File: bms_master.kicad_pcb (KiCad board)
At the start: 4 copper layers, 85 x 65 mm, 104 parts, among them J1 Conn_01x02, J2 Conn_01x02, J3 Conn_01x02, J4 Conn_01x04, J5 Conn_01x04, J6 Conn_01x06, J7 Conn_01x05, J8 Conn_01x05, Q1 PMV15ENE, Q2 PMV74EPE, Q3 PMV74EPE, SW1 SW_Push, U1 TPS7B88, U10 TPS3851, U2 MCP1700x-330xxMB, U3 STM32F103C8Tx, U4 SN65HVD1050D, U5 M24C64-R, U6 MAX6126, U7 MAX11163, U8 741G3157, U9 TPS25961, Y1 8M

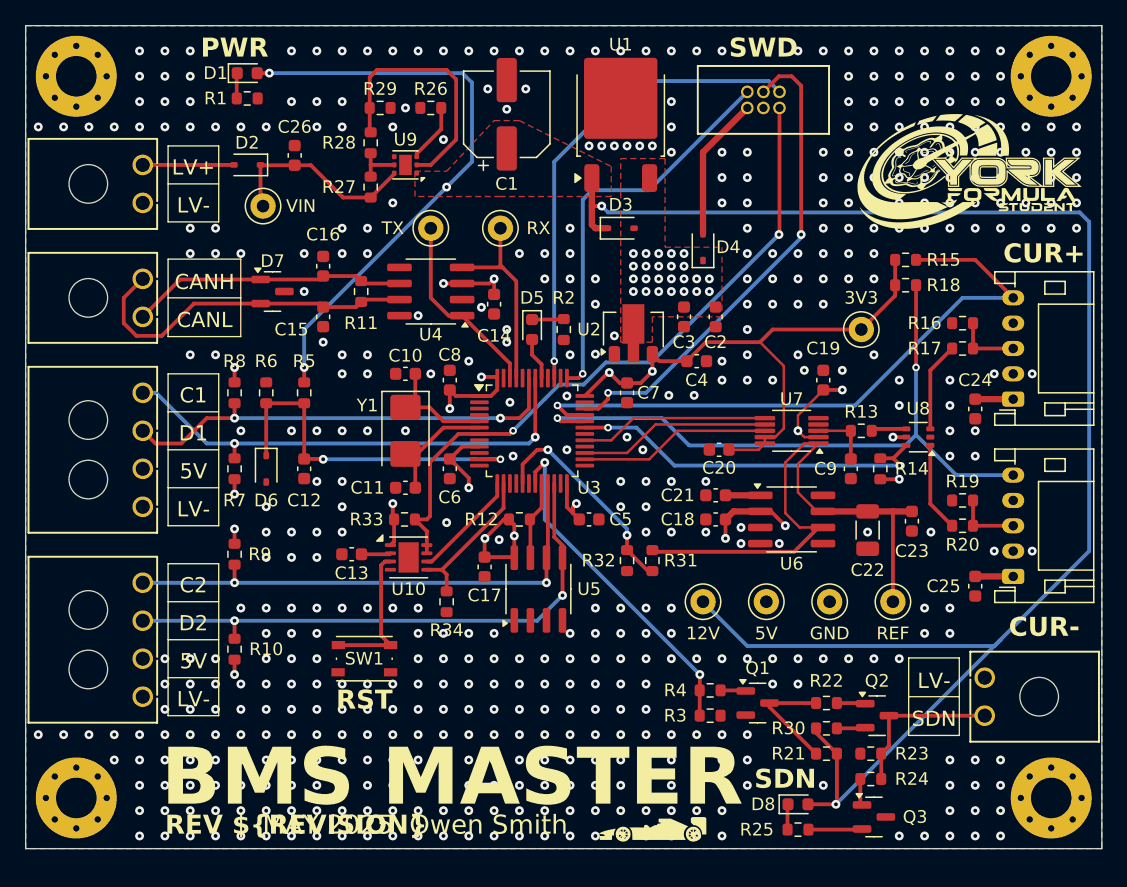
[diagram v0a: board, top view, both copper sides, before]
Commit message: pcb: Cleanup connector silkscreen
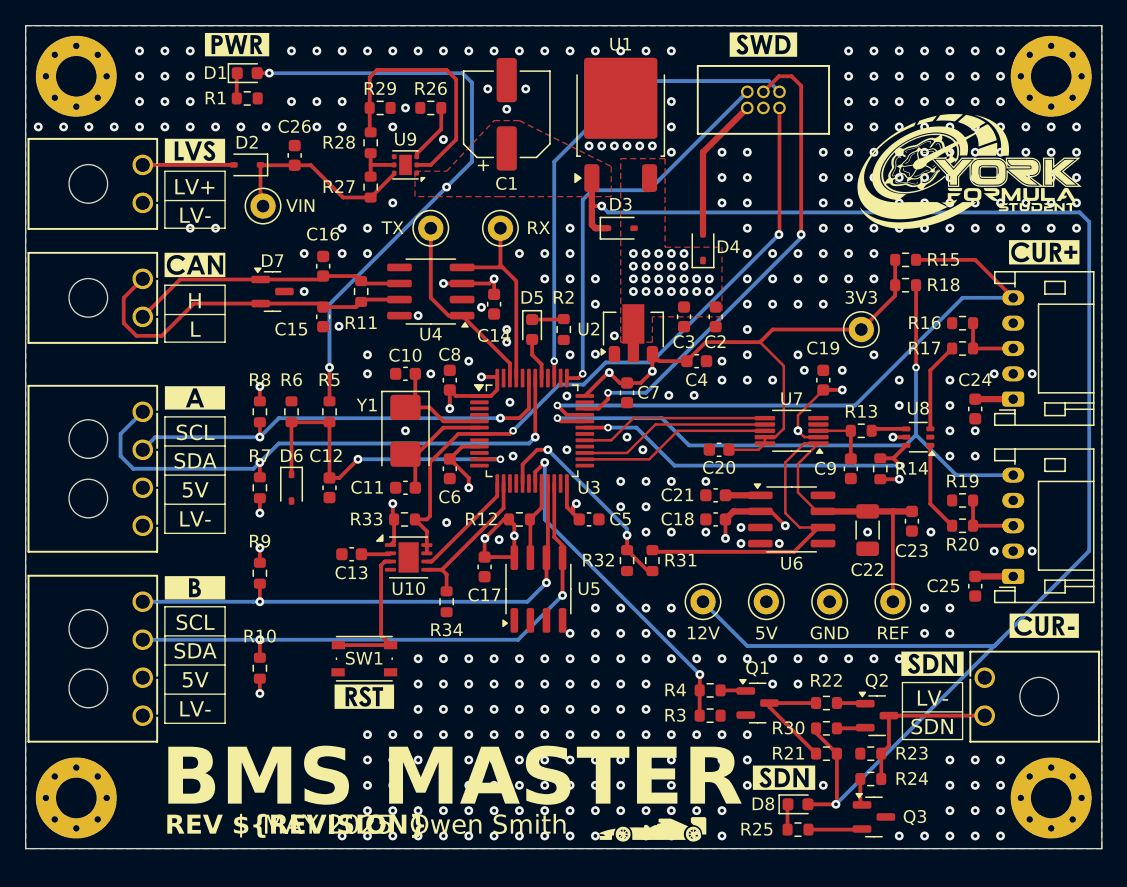
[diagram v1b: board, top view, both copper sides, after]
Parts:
- added kibuzzard-6910B743: G***, kibuzzard-6910B743, F.Cu at (78.4, 48.9)
- added kibuzzard-6910B7D7: G***, kibuzzard-6910B7D7, F.Cu at (78.4, 39.9)
- added kibuzzard-6910B84D: G***, kibuzzard-6910B84D, F.Cu at (78.4, 59.4)
- added kibuzzard-6910B859: G***, kibuzzard-6910B859, F.Cu at (78.4, 74.4)
- added kibuzzard-6910B9F6: G***, kibuzzard-6910B9F6, F.Cu at (124.9, 89.4)
- added kibuzzard-6910B9F6: G***, kibuzzard-6910B9F6, F.Cu at (136.6, 80.4)
- added kibuzzard-6910BA67: G***, kibuzzard-6910BA67, F.Cu at (145.4, 47.9)
- added kibuzzard-6910BA7C: G***, kibuzzard-6910BA7C, F.Cu at (145.4, 77.4)
- added kibuzzard-6910BB45: G***, kibuzzard-6910BB45, F.Cu at (91.8, 83.0)
- added kibuzzard-6910BB6B: G***, kibuzzard-6910BB6B, F.Cu at (81.7, 31.5)
- added kibuzzard-6910BB76: G***, kibuzzard-6910BB76, F.Cu at (123.3, 31.5)
- moved C12 2.50 mm to (89.0, 66.5)
- moved D6 2.50 mm to (86.0, 66.5)
- moved R10 2.50 mm to (83.5, 80.8)
- moved R5 2.50 mm to (89.0, 60.5)
- moved R6 2.50 mm to (86.0, 60.5)
- moved R7 2.50 mm to (83.5, 66.5)
- moved R8 2.50 mm to (83.5, 60.5)
- moved R9 2.50 mm to (83.5, 73.2)
- moved J4 1.50 mm to (74.2, 69.5)
- moved J5 1.50 mm to (74.2, 84.5)
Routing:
- net SCL1: track 38.7 -> 44.3 mm
- net Net-(D6-K): track 28.7 -> 27.3 mm
- net +12V: track 179.6 -> 180.3 mm
- net SDA2: track 44.5 -> 45.1 mm
- net SCL2: track 41.2 -> 41.8 mm
- net GND: vias 495 -> 378
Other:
- board text added: "H"
- board text added: "L"
- board text added: "SCL"
- board text added: "SDA"
- board text removed: "C1"
- board text removed: "C2"
- board text removed: "CANH"
- board text removed: "CANL"
- board text removed: "CUR+"
- board text removed: "CUR-"
- board text removed: "D1"
- board text removed: "D2"
- board text removed: "PWR"
- board text removed: "RST"
- board text removed: "SWD"

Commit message: *: Reorder reference designators
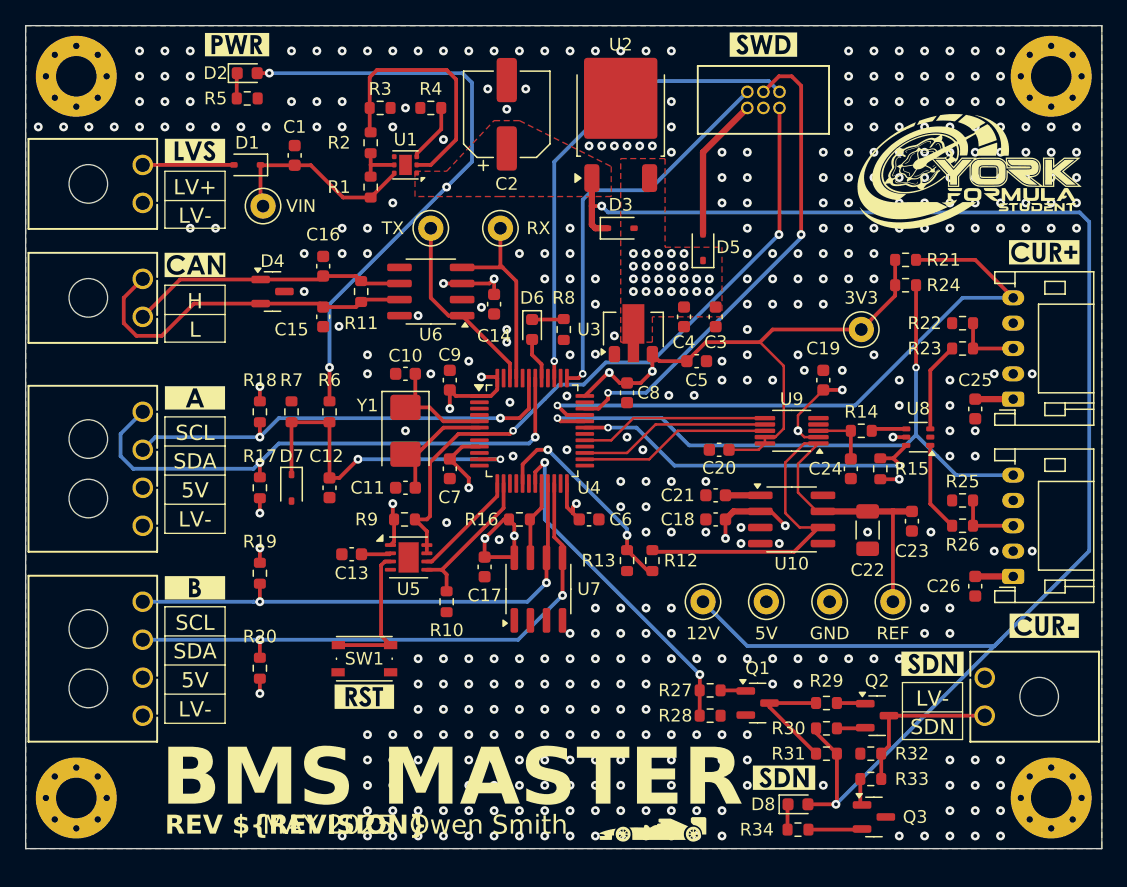
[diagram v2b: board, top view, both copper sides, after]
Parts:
- renumbered C26 to C1, C1 to C2, C9 to C24, C24 to C25, C25 to C26, C2 to C3, C3 to C4, C4 to C5, C5 to C6, C6 to C7, C7 to C8, C8 to C9, D2 to D1, D1 to D2, D7 to D4, D4 to D5, D5 to D6, D6 to D7, R27 to R1, R34 to R10, R31 to R12, R32 to R13, R13 to R14, R14 to R15, R12 to R16, R7 to R17, R8 to R18, R9 to R19, R28 to R2, R10 to R20, R15 to R21, R16 to R22, R17 to R23, R18 to R24, R19 to R25, R20 to R26, R4 to R27, R3 to R28, R22 to R29, R29 to R3, R21 to R31, R23 to R32, R24 to R33, R25 to R34, R26 to R4, R1 to R5, R5 to R6, R6 to R7, R2 to R8, R33 to R9, U9 to U1, U6 to U10, U1 to U2, U2 to U3, U3 to U4, U10 to U5, U4 to U6, U5 to U7, U7 to U9

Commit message: pcb: Cleanup vias and designator silkscreen
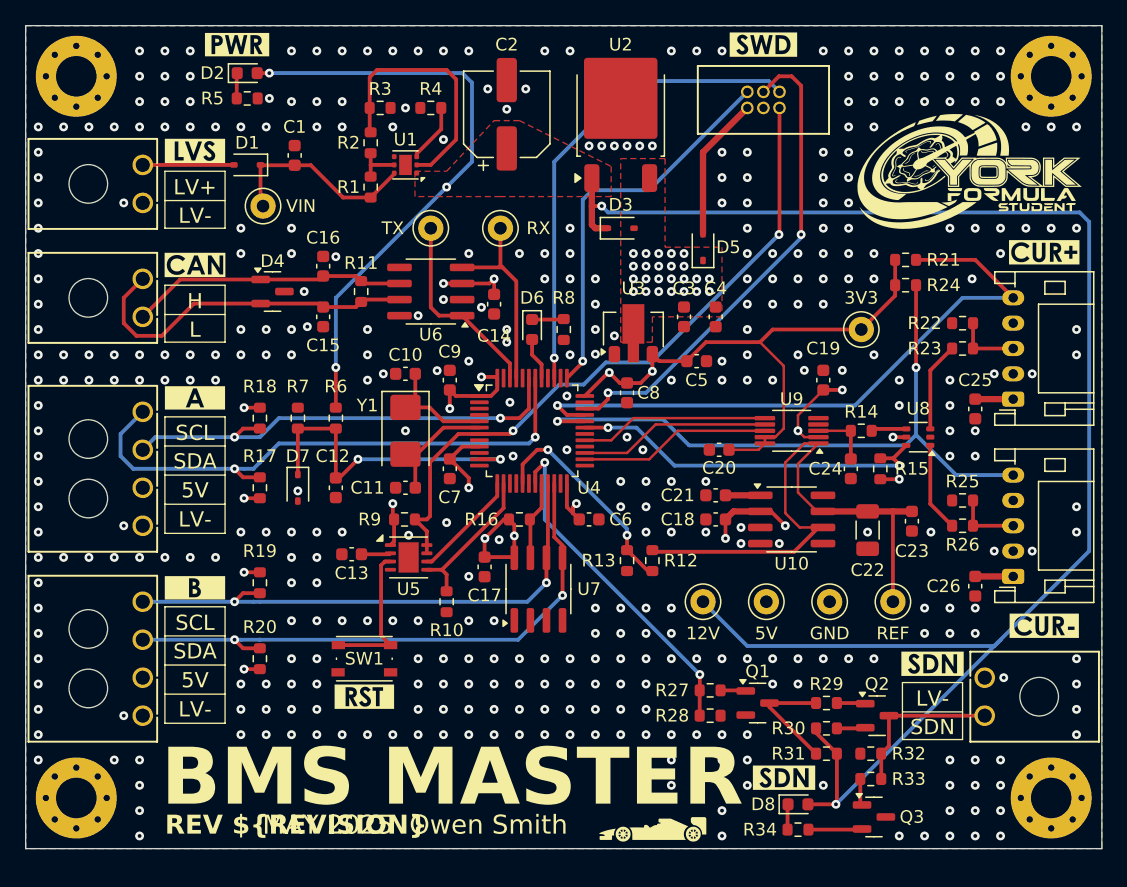
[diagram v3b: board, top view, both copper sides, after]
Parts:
- moved C3 2.50 mm to (117.0, 53.0)
- moved C4 2.50 mm to (119.5, 53.0)
- moved R19 0.75 mm to (83.5, 74.0)
- moved R20 0.75 mm to (83.5, 80.0)
- moved R6 0.71 mm to (89.5, 61.0)
- moved R7 0.71 mm to (86.5, 61.0)
- moved C12 0.50 mm to (89.5, 66.5)
- moved D7 0.50 mm to (86.5, 66.5)
- moved R18 0.50 mm to (83.5, 61.0)
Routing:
- net Net-(D7-K): track 27.3 -> 25.8 mm
- net SCL1: track 44.3 -> 45.4 mm
- net SDA1: track 35.4 -> 36.5 mm
- net SDA2: track 45.1 -> 46.0 mm
- net SCL2: track 41.8 -> 42.7 mm
- net /SWCLK: track 31.7 -> 31.1 mm
- net GND: vias 378 -> 395

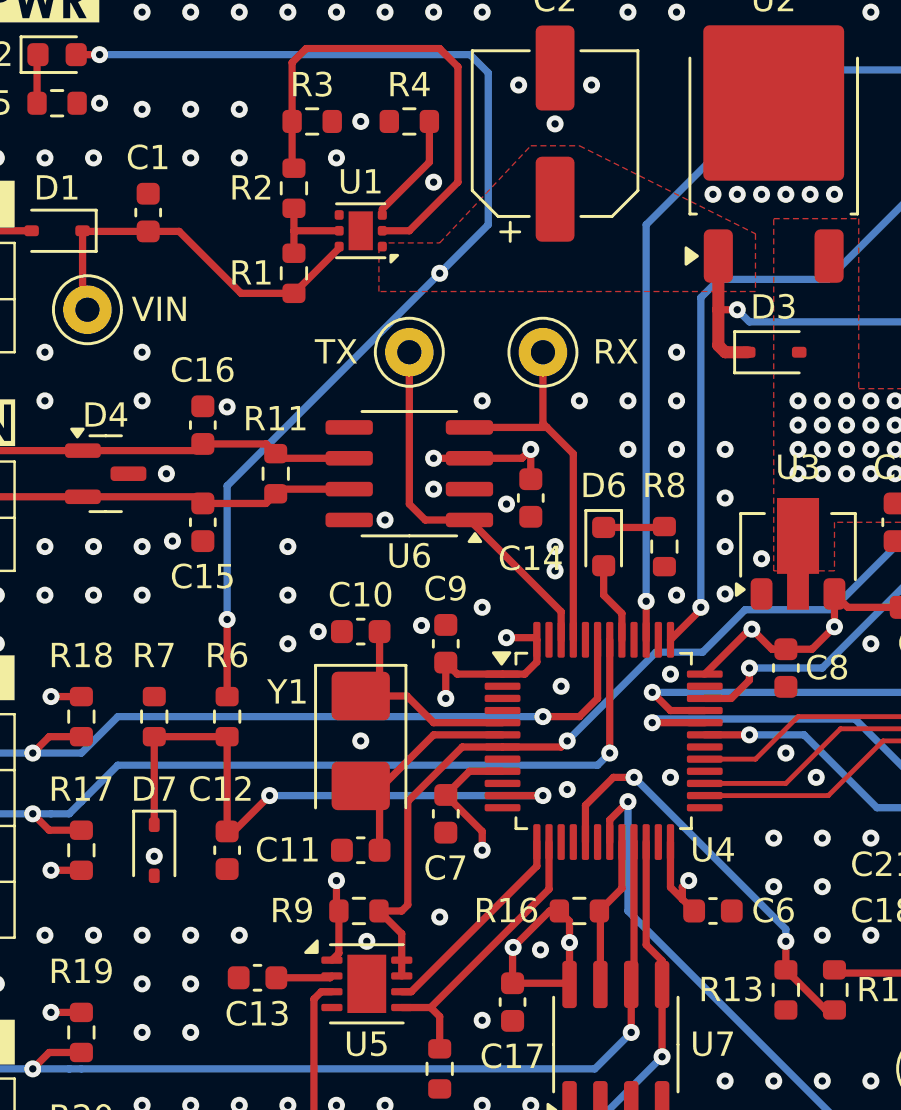
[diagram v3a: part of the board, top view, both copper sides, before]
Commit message: pcb: Cleanup some empty islands
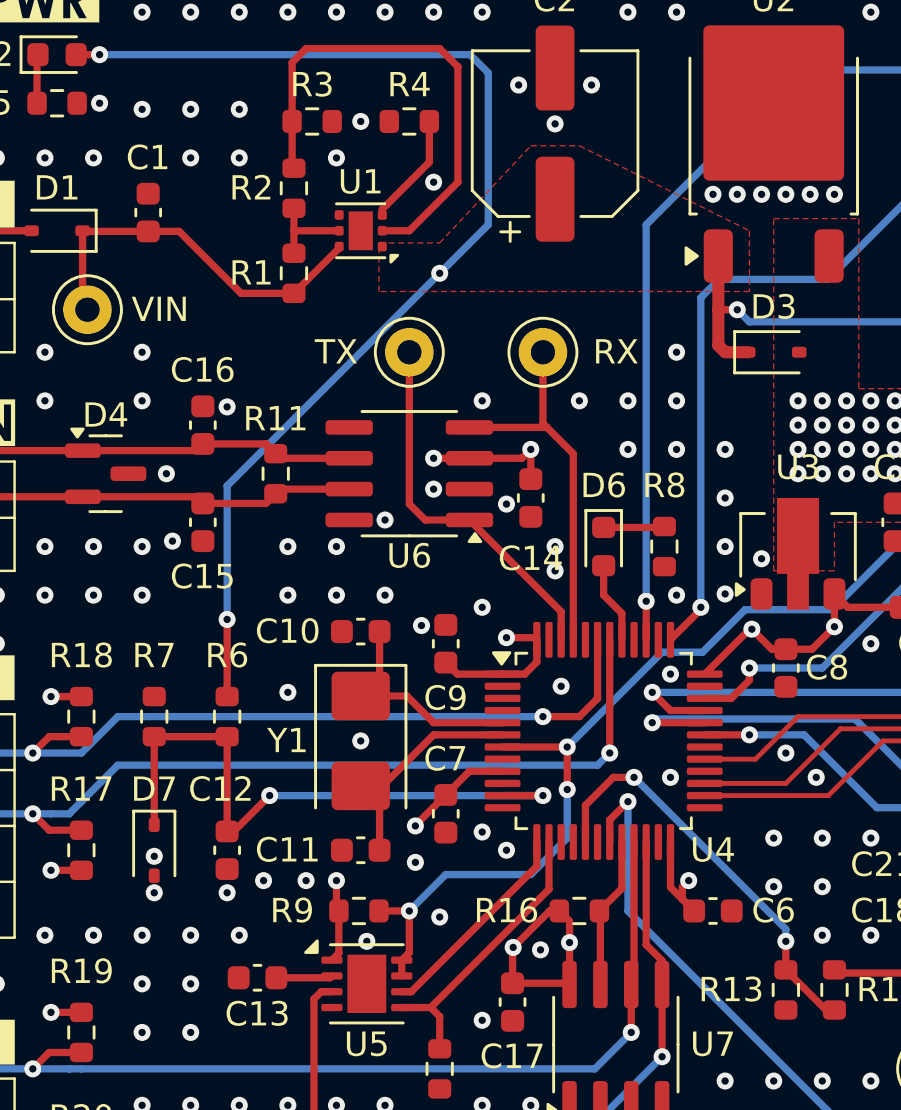
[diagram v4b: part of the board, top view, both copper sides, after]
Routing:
- net +3V3: track 66.5 -> 63.9 mm, vias 7 -> 6
- net NRST: track 53.6 -> 55.8 mm, vias 2 -> 4
- net GND: vias 395 -> 403
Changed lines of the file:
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@@
 		(descr "SMD2520/2, Crystal, 5.0x3.2mm package, SMD, generated with kicad-footprint-generator make_crystal.py, http://www.icbase.com/File/PDF/HKC/HKC00061008.pdf")
 		(property "Reference" "Y1"
-			(at -2 3 180)
+			(at 0 3 180)
 			(layer "F.SilkS")
 			(effects
@@
 		(tags "capacitor")
 		(property "Reference" "C9"
-			(at 2.25 0 180)
+			(at -2.25 0 180)
 			(layer "F.SilkS")
 			(effects
@@
 		(tags "capacitor")
 		(property "Reference" "C10"
-			(at 0 -1.5 0)
+			(at -3 0 0)
 			(layer "F.SilkS")
 			(effects
@@
 		(tags "capacitor")
 		(property "Reference" "C7"
-			(at 2.25 0 180)
+			(at -2.25 0 180)
 			(layer "F.SilkS")
 			(effects
@@
 	)
 	(via
-		(at 103.5 64)
-		(size 0.7)
-		(drill 0.3)
-		(layers "F.Cu" "B.Cu")
-		(free yes)
-		(net 1)
-	)
-	(via
 		(at 128 32)
 		(size 0.7)
@@
 	)
 	(via
+		(at 92.75 67.75)
+		(size 0.7)
+		(drill 0.3)
+		(layers "F.Cu" "B.Cu")
+		(free yes)
+		(net 1)
+	)
+	(via
 		(at 92 86)
 		(size 0.7)
@@
 	)
 	(via
+		(at 101 66.5)
+		(size 0.7)
+		(drill 0.3)
+		(layers "F.Cu" "B.Cu")
+		(free yes)
+		(net 1)
+	)
+	(via
 		(at 128 42)
 		(size 0.7)
@@
 	)
 	(via
+		(at 91 67.75)
+		(size 0.7)
+		(drill 0.3)
+		(layers "F.Cu" "B.Cu")
+		(free yes)
+		(net 1)
+	)
+	(via
 		(at 116 70)
 		(size 0.7)
@@
 	)
 	(via
+		(at 100 65.75)
+		(size 0.7)
+		(drill 0.3)
+		(layers "F.Cu" "B.Cu")
+		(free yes)
+		(net 1)
+	)
+	(via
 		(at 94 86)
 		(size 0.7)
@@
 	)
 	(via
+		(at 89.5 68.25)
+		(size 0.7)
+		(drill 0.3)
+		(layers "F.Cu" "B.Cu")
+		(free yes)
+		(net 1)
+	)
+	(via
 		(at 148 84)
 		(size 0.7)
@@
 	)
 	(via
-		(at 92 58)
-		(size 0.7)
-		(drill 0.3)
-		(layers "F.Cu" "B.Cu")
-		(free yes)
-		(net 1)
-	)
-	(via
 		(at 110 52)
 		(size 0.7)
@@
 	)
 	(via
+		(at 92 60)
+		(size 0.7)
+		(drill 0.3)
+		(layers "F.Cu" "B.Cu")
+		(free yes)
+		(net 1)
+	)
+	(via
 		(at 132 36)
 		(size 0.7)
@@
 	)
 	(via
+		(at 94 54)
+		(size 0.7)
+		(drill 0.3)
+		(layers "F.Cu" "B.Cu")
+		(free yes)
+		(net 1)
+	)
+	(via
 		(at 66 78)
 		(size 0.7)
@@
 	)
 	(via
+		(at 96 56)
+		(size 0.7)
+		(drill 0.3)
+		(layers "F.Cu" "B.Cu")
+		(free yes)
+		(net 1)
+	)
+	(via
 		(at 72.75 44)
 		(size 0.7)
@@
 	)
 	(via
+		(at 86.5 68.25)
+		(size 0.7)
+		(drill 0.3)
+		(layers "F.Cu" "B.Cu")
+		(free yes)
+		(net 1)
+	)
+	(via
 		(at 112 84)
 		(size 0.7)
@@
 	)
 	(via
+		(at 94 56)
+		(size 0.7)
+		(drill 0.3)
+		(layers "F.Cu" "B.Cu")
+		(free yes)
+		(net 1)
+	)
+	(via
 		(at 74 90)
 		(size 0.7)
@@
 	)
 	(via
+		(at 97.25 67)
+		(size 0.7)
+		(drill 0.3)
+		(layers "F.Cu" "B.Cu")
+		(free yes)
+		(net 1)
+	)
+	(via
 		(at 140 34)
 		(size 0.7)
@@
 	)
 	(via
-		(at 93.25 57.5)
-		(size 0.7)
-		(drill 0.3)
-		(layers "F.Cu" "B.Cu")
-		(free yes)
-		(net 1)
-	)
-	(via
 		(at 138 36)
 		(size 0.7)
@@
 	)
 	(segment
+		(start 97.25 65.475)
+		(end 98.5 64.225)
+		(width 0.3)
+		(layer "F.Cu")
+		(net 4)
+	)
+	(segment
 		(start 111.925 58.225)
 		(end 111.1 57.4)
@@
 	)
 	(segment
-		(start 98.5 60.25)
-		(end 98.5 58.775)
-		(width 0.3)
-		(layer "F.Cu")
-		(net 4)
-	)
-	(segment
 		(start 101 57.75)
 		(end 102.1625 57.75)
@@
 	)
 	(segment
-		(start 98.5 64.225)
-		(end 100 65.725)
-		(width 0.3)
-		(layer "F.Cu")
-		(net 4)
-	)
-	(segment
 		(start 131 54)
 		(end 124 54)
@@
 	)
 	(segment
-		(start 100 65.725)
-		(end 100 66.5)
+		(start 97.25 65.5)
+		(end 97.25 65.475)
 		(width 0.3)
 		(layer "F.Cu")
@@
 	)
 	(via
-		(at 98.5 60.25)
-		(size 0.7)
-		(drill 0.3)
-		(layers "F.Cu" "B.Cu")
-		(free yes)
-		(net 4)
-	)
-	(via
 		(at 101 57.75)
 		(size 0.7)
@@
 	)
 	(via
-		(at 114.5 57.3)
+		(at 97.25 65.5)
 		(size 0.7)
 		(drill 0.3)
@@
 	)
 	(via
-		(at 111.1 57.4)
+		(at 114.5 57.3)
 		(size 0.7)
 		(drill 0.3)
@@
 	)
 	(via
-		(at 100 66.5)
+		(at 111.1 57.4)
 		(size 0.7)
 		(drill 0.3)
@@
 	)
 	(segment
-		(start 96.6875 69)
-		(end 95.75 69)
-		(width 0.3)
-		(layer "F.Cu")
-		(net 68)
-	)
-	(segment
-		(start 96.9375 68.75)
-		(end 96.6875 69)
-		(width 0.3)
-		(layer "F.Cu")
-		(net 68)
-	)
-	(segment
-		(start 103.25 62.25)
-		(end 103.5 62)
-		(width 0.3)
-		(layer "F.Cu")
-		(net 68)
-	)
-	(segment
-		(start 100.8375 62.25)
-		(end 103.25 62.25)
+		(start 96.6875 71.025)
+		(end 97 70.7125)
 		(width 0.3)
 		(layer "F.Cu")
@@
 	)
 	(segment
-		(start 95.75 69)
-		(end 96.6875 69.9375)
+		(start 97 70.7125)
+		(end 97 69)
 		(width 0.3)
 		(layer "F.Cu")
@@
 	)
 	(segment
-		(start 99.179178 62.25)
-		(end 96.9375 64.491678)
+		(start 100.8375 62.25)
+		(end 103.5 62.25)
 		(width 0.3)
 		(layer "F.Cu")
@@
 	)
 	(segment
-		(start 100.8375 62.25)
-		(end 99.179178 62.25)
+		(start 103.5 64)
+		(end 103.5 62.25)
 		(width 0.3)
 		(layer "F.Cu")
@@
 	)
 	(segment
-		(start 96.9375 64.491678)
-		(end 96.9375 68.75)
+		(start 97 69)
+		(end 95.75 69)
 		(width 0.3)
 		(layer "F.Cu")
@@
 		(net 68)
 	)
-	(segment
-		(start 96.6875 69.9375)
-		(end 96.6875 71.025)
-		(width 0.3)
-		(layer "F.Cu")
+	(via
+		(at 97 69)
+		(size 0.7)
+		(drill 0.3)
+		(layers "F.Cu" "B.Cu")
+		(free yes)
+		(net 68)
+	)
+	(via
+		(at 103.5 64)
+		(size 0.7)
+		(drill 0.3)
+		(layers "F.Cu" "B.Cu")
+		(free yes)
 		(net 68)
 	)
@@
 	)
 	(via
-		(at 103.5 62)
+		(at 103.5 62.25)
 		(size 0.7)
 		(drill 0.3)
@@
 	)
 	(segment
-		(start 107.151 58.349)
-		(end 103.5 62)
+		(start 97 69)
+		(end 98.5 67.5)
+		(width 0.3)
+		(layer "B.Cu")
+		(net 68)
+	)
+	(segment
+		(start 103.5 66)
+		(end 103.5 64)
 		(width 0.3)
 		(layer "B.Cu")
@@
 	)
 	(segment
+		(start 98.5 67.5)
+		(end 102 67.5)
+		(width 0.3)
+		(layer "B.Cu")
+		(net 68)
+	)
+	(segment
+		(start 102 67.5)
+		(end 103.5 66)
+		(width 0.3)
+		(layer "B.Cu")
+		(net 68)
+	)
+	(segment
 		(start 109.071654 58.349)
-		(end 107.151 58.349)
+		(end 107.401 58.349)
+		(width 0.3)
+		(layer "B.Cu")
+		(net 68)
+	)
+	(segment
+		(start 107.401 58.349)
+		(end 103.5 62.25)
 		(width 0.3)
 		(layer "B.Cu")
@@
 		(polygon
 			(pts
-				(xy 98.25 41.5) (xy 102 37.5) (xy 104 37.5) (xy 111.25 41.125) (xy 111.25 43.5) (xy 102.666667 43.5)
-				(xy 102.5 43.5) (xy 97.25 43.5) (xy 95.75 43.5) (xy 95.75 41.5)
+				(xy 98.25 41.5) (xy 102 37.5) (xy 104 37.5) (xy 111 41) (xy 111 43.5) (xy 102.666667 43.5) (xy 102.5 43.5)
+				(xy 97.25 43.5) (xy 95.75 43.5) (xy 95.75 41.5)
 			)
 		)
